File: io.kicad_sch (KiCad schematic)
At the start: 17 parts, among them J2 USB_C_Receptacle_USB2.0_14P, U3 FT2232HL, Y1 12Mhz

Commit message: Power rail stuff
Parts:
- added J2: Micro_SD_Card, symbol Connector:Micro_SD_Card
- renumbered J2 to J1
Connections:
- net GND: now also J2.SH (SHIELD)

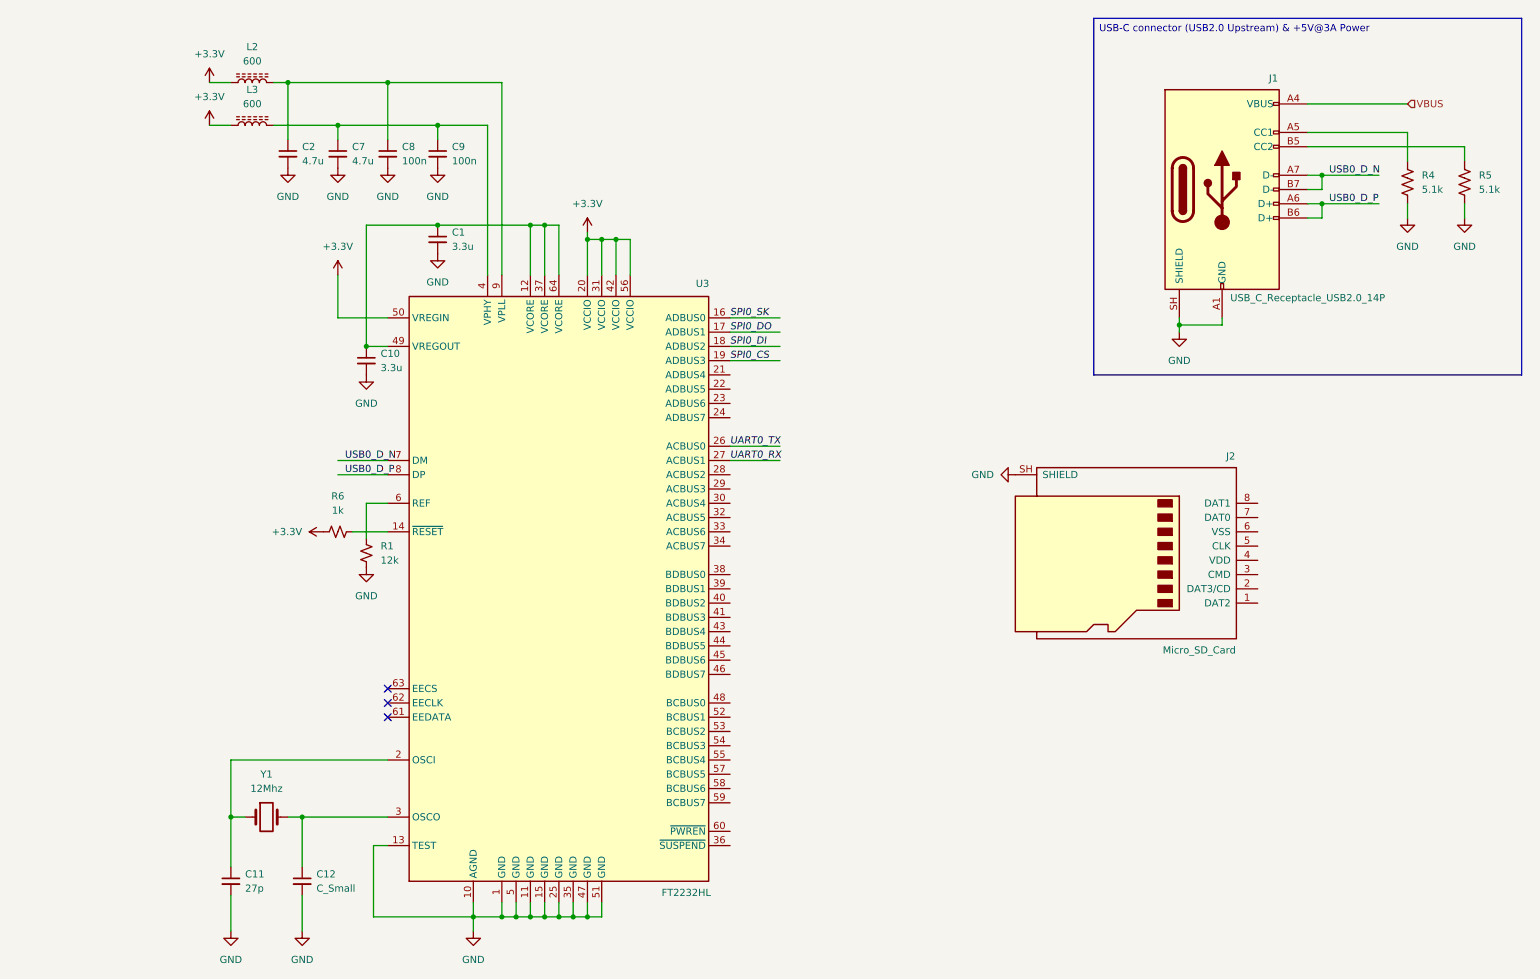
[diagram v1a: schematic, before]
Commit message: Fixed regulator, started wiring the microSD & MCU
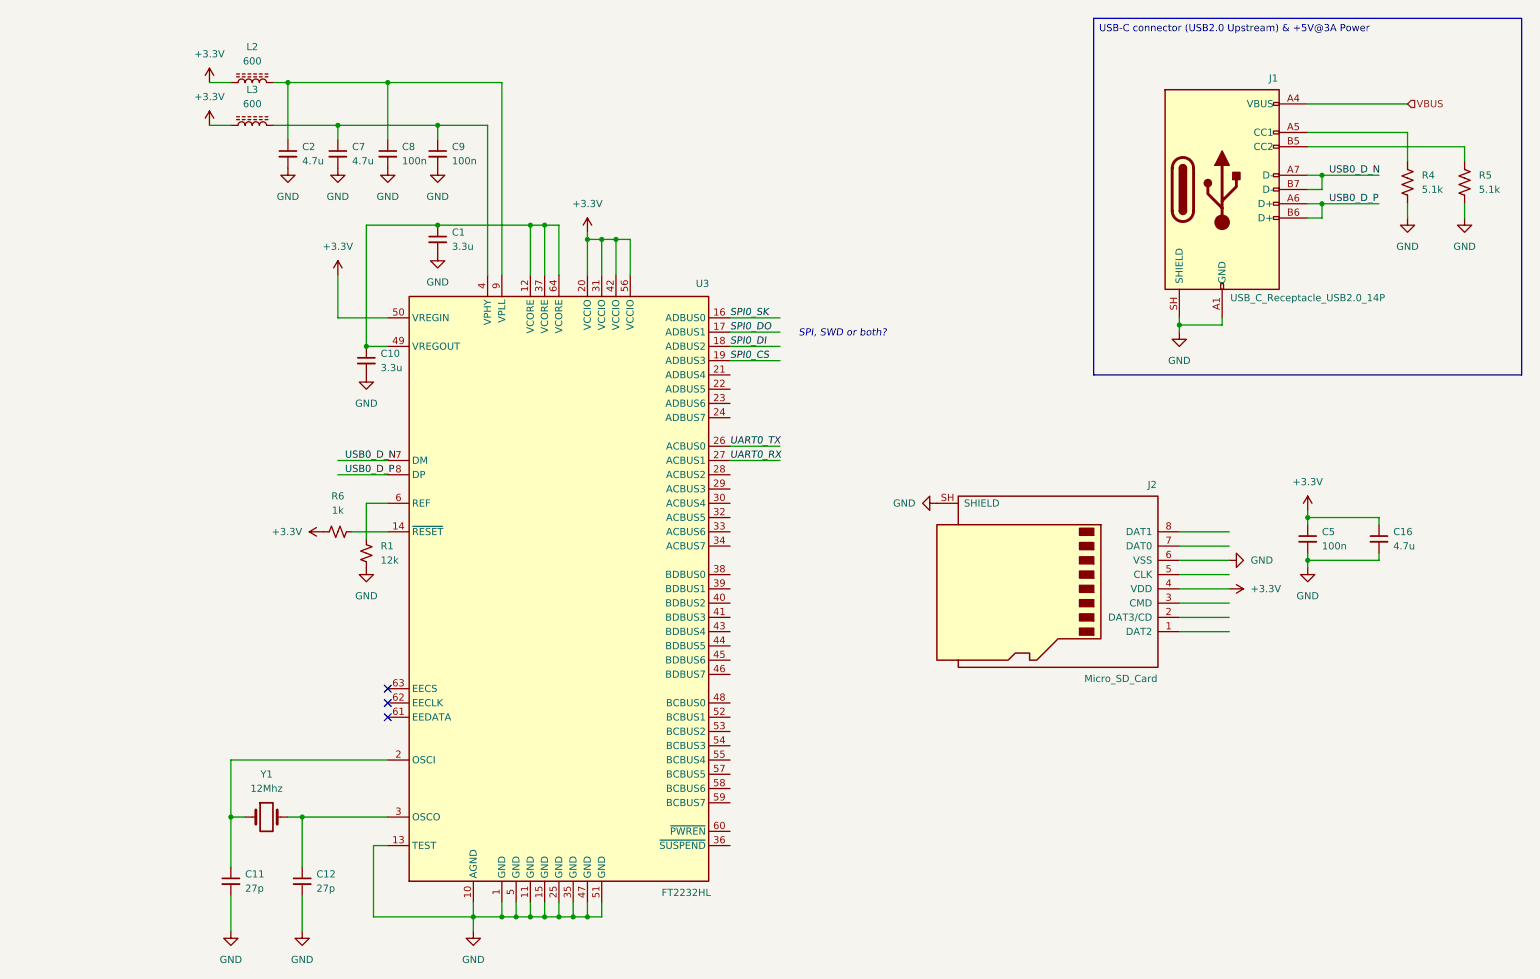
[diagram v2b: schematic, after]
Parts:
- added C16: 4.7u, symbol Device:C_Small
- added C5: 100n, symbol Device:C_Small
- C12: value C_Small -> 27p
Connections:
- net +3.3V: now also J2.4 (VDD), C16.1, C5.1
- net GND: now also J2.6 (VSS), C16.2, C5.2
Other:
- note added: "SPI, SWD or both?"
- moved on the sheet: J2

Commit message: MCU wiring
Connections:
- net SD0_DAT2: now reaches J2.1 (DAT2)
- net SD0_DAT3: now reaches J2.2 (DAT3/CD)
- net SD0_CMD: now reaches J2.3 (CMD)
- net SD0_CLK: now reaches J2.5 (CLK)
- net SD0_DAT0: now reaches J2.7 (DAT0)
- net SD0_DAT1: now reaches J2.8 (DAT1)
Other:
- moved on the sheet: C16, C5, J2

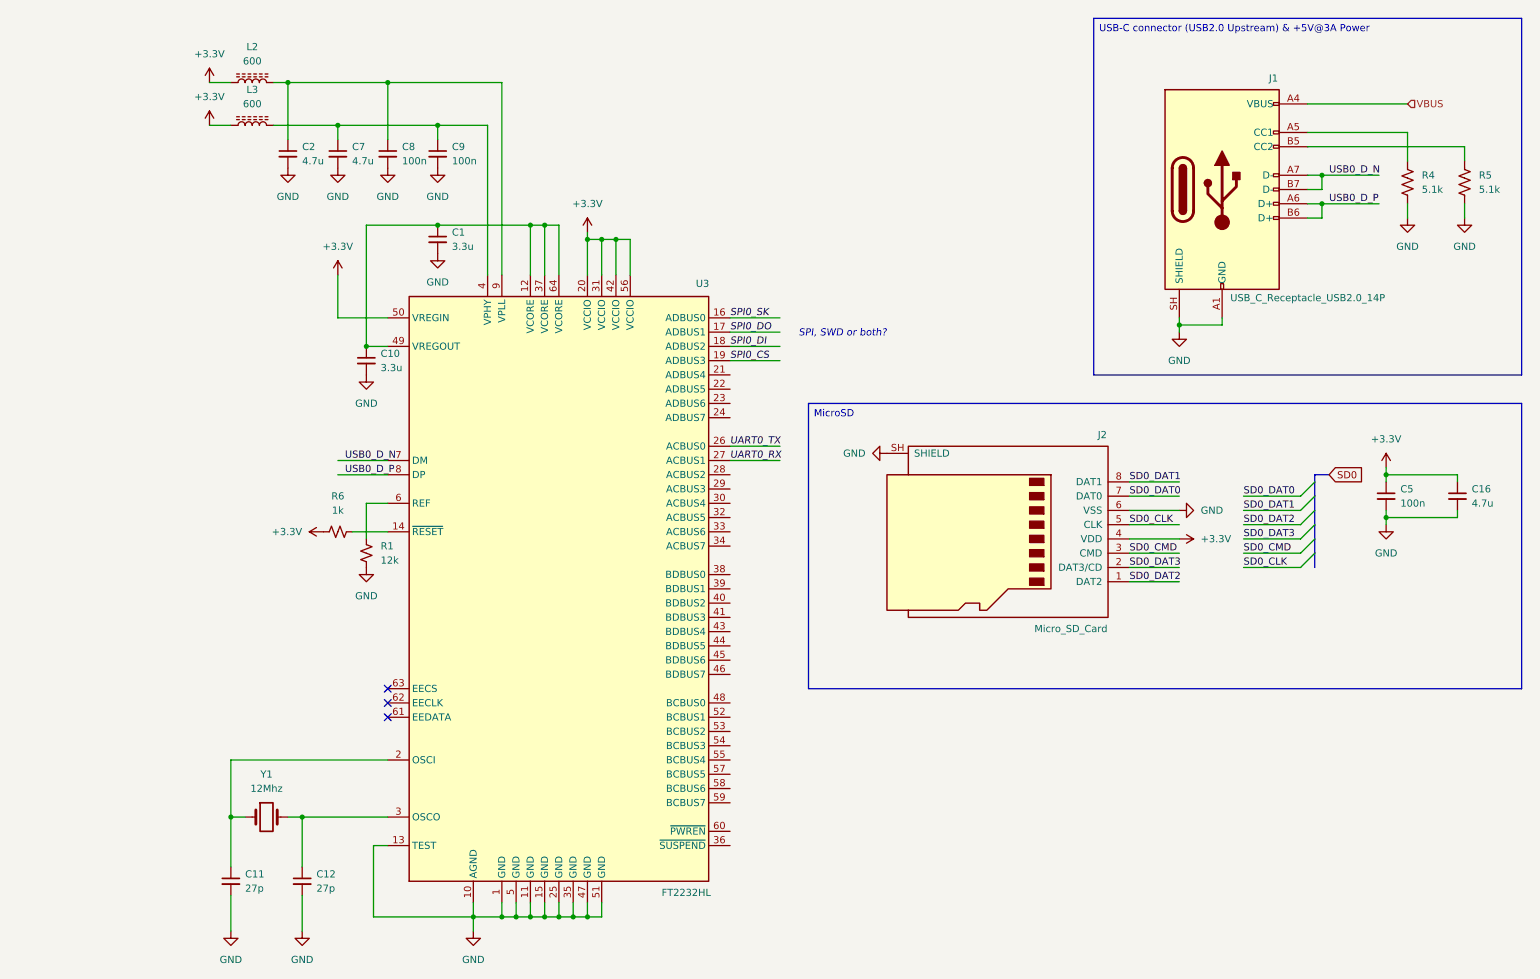
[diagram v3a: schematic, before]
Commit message: Minor re-organization and additional power filtering
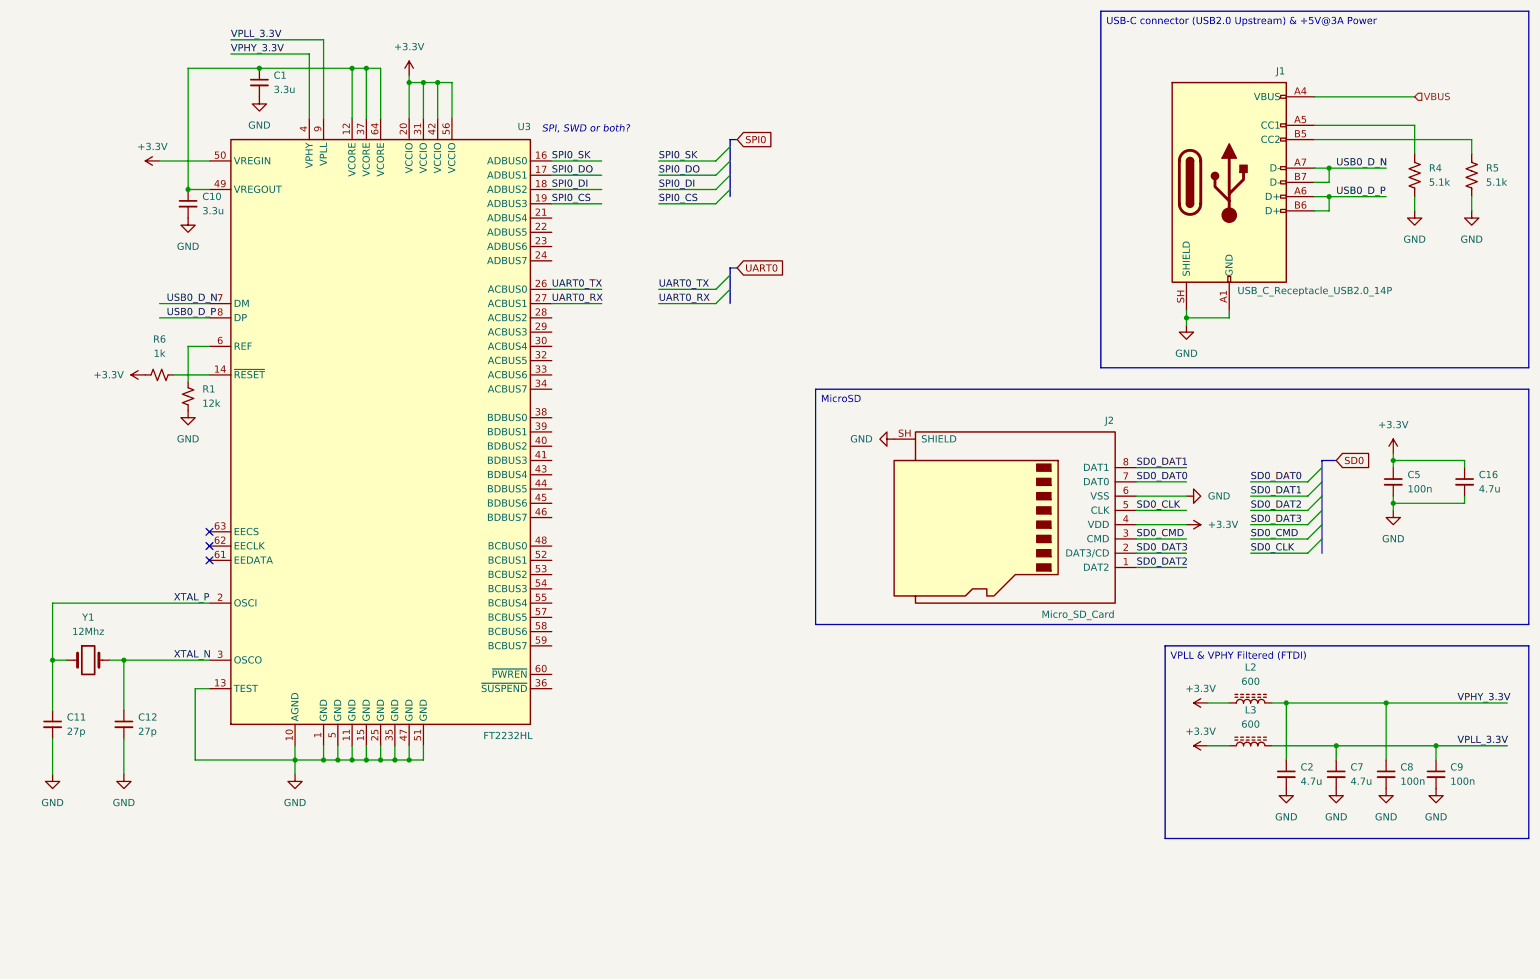
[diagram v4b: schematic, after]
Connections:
- net VPHY_3.3V: now reaches C2.1, C8.1, L2.2
- net VPHY_3.3V: now also U3.4 (VPHY); no longer U3.9 (VPLL)
- net XTAL_P: now reaches C11.1, U3.2 (OSCI), Y1.1
- net XTAL_N: now reaches C12.1, U3.3 (OSCO), Y1.2
- net VPLL_3.3V: now reaches C7.1, C9.1, L3.2
- net VPLL_3.3V: now also U3.9 (VPLL); no longer U3.4 (VPHY)
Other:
- moved on the sheet: C1, C10, C11, C12, C16, C2, C5, C7, C8, C9, J1, J2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

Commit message: Minor
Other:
- note added: "TODO: Load caps depend on XTAL model"
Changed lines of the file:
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@@
+		)
+	)
+	(text "TODO: Load caps depend on XTAL model"
+		(exclude_from_sim no)
+		(at 34.29 160.782 0)
+		(effects
+			(font
+				(size 1.27 1.27)
+				(italic yes)
+			)
 		)
 	)

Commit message: Minor
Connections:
- net GND: no longer J1.SH (SHIELD)
- no-connect marks 3 -> 4
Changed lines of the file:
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@@
 	)
 	(junction
-		(at 220.98 69.85)
-		(diameter 0)
-		(color 0 0 0 0)
-	)
-	(junction
 		(at 19.05 130.81)
 		(diameter 0)
@@
 	)
 	(no_connect
+		(at 220.98 68.58)
+	)
+	(no_connect
 		(at 46.99 110.49)
 	)
@@
 	(wire
 		(pts
-			(xy 220.98 69.85) (xy 220.98 71.12)
-		)
-		(stroke
-			(width 0)
-			(type default)
-		)
-	)
-	(wire
-		(pts
 			(xy 80.01 146.05) (xy 80.01 148.59)
 		)
@@
 	(wire
 		(pts
-			(xy 220.98 69.85) (xy 228.6 69.85)
-		)
-		(stroke
-			(width 0)
-			(type default)
-		)
-	)
-	(wire
-		(pts
-			(xy 220.98 68.58) (xy 220.98 69.85)
-		)
-		(stroke
-			(width 0)
-			(type default)
-		)
-	)
-	(wire
-		(pts
 			(xy 127 67.31) (xy 137.16 67.31)
 		)
@@
 		)
 	)
+	(global_label "VBUS"
+		(shape input)
+		(at 261.62 30.48 0)
+		(fields_autoplaced yes)
+		(effects
+			(font
+				(size 1.27 1.27)
+			)
+			(justify left)
+		)
+		(property "Intersheetrefs" "${INTERSHEET_REFS}"
+			(at 268.5467 30.48 0)
+			(hide yes)
+			(show_name no)
+			(do_not_autoplace no)
+			(effects
+				(font
+					(size 1.27 1.27)
+				)
+				(justify left)
+			)
+		)
+	)
 	(global_label "UART0"
 		(shape input)
@@
 		)
 	)
-	(hierarchical_label "VBUS"
-		(shape input)
-		(at 261.62 30.48 0)
-		(effects
-			(font
-				(size 1.27 1.27)
-			)
-			(justify left)
-		)
-	)
 	(symbol
 		(lib_id "power:GND")
@@
 	(symbol
 		(lib_id "power:GND")
-		(at 220.98 71.12 0)
+		(at 228.6 69.85 0)
 		(unit 1)
 		(body_style 1)
@@
 		(fields_autoplaced yes)
 		(property "Reference" "#PWR016"
-			(at 220.98 77.47 0)
+			(at 228.6 76.2 0)
 			(hide yes)
 			(show_name no)
@@
 		)
 		(property "Value" "GND"
-			(at 220.98 76.2 0)
+			(at 228.6 74.93 0)
 			(show_name no)
 			(do_not_autoplace no)
@@
 		)
 		(property "Footprint" ""
-			(at 220.98 71.12 0)
+			(at 228.6 69.85 0)
 			(hide yes)
 			(show_name no)
@@
 		)
 		(property "Datasheet" ""
-			(at 220.98 71.12 0)
+			(at 228.6 69.85 0)
 			(hide yes)
 			(show_name no)
@@
 		)
 		(property "Description" "Power symbol creates a global label with name \"GND\" , ground"
-			(at 220.98 71.12 0)
+			(at 228.6 69.85 0)
 			(hide yes)
 			(show_name no)
